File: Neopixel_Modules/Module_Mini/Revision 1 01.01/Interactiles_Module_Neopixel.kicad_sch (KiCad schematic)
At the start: 29 parts, among them J1 PINHD_1x2_Male, J2 PINHD_1x2_Female, J4 PINHD_1x2_Female, U1 MCP23017_ML

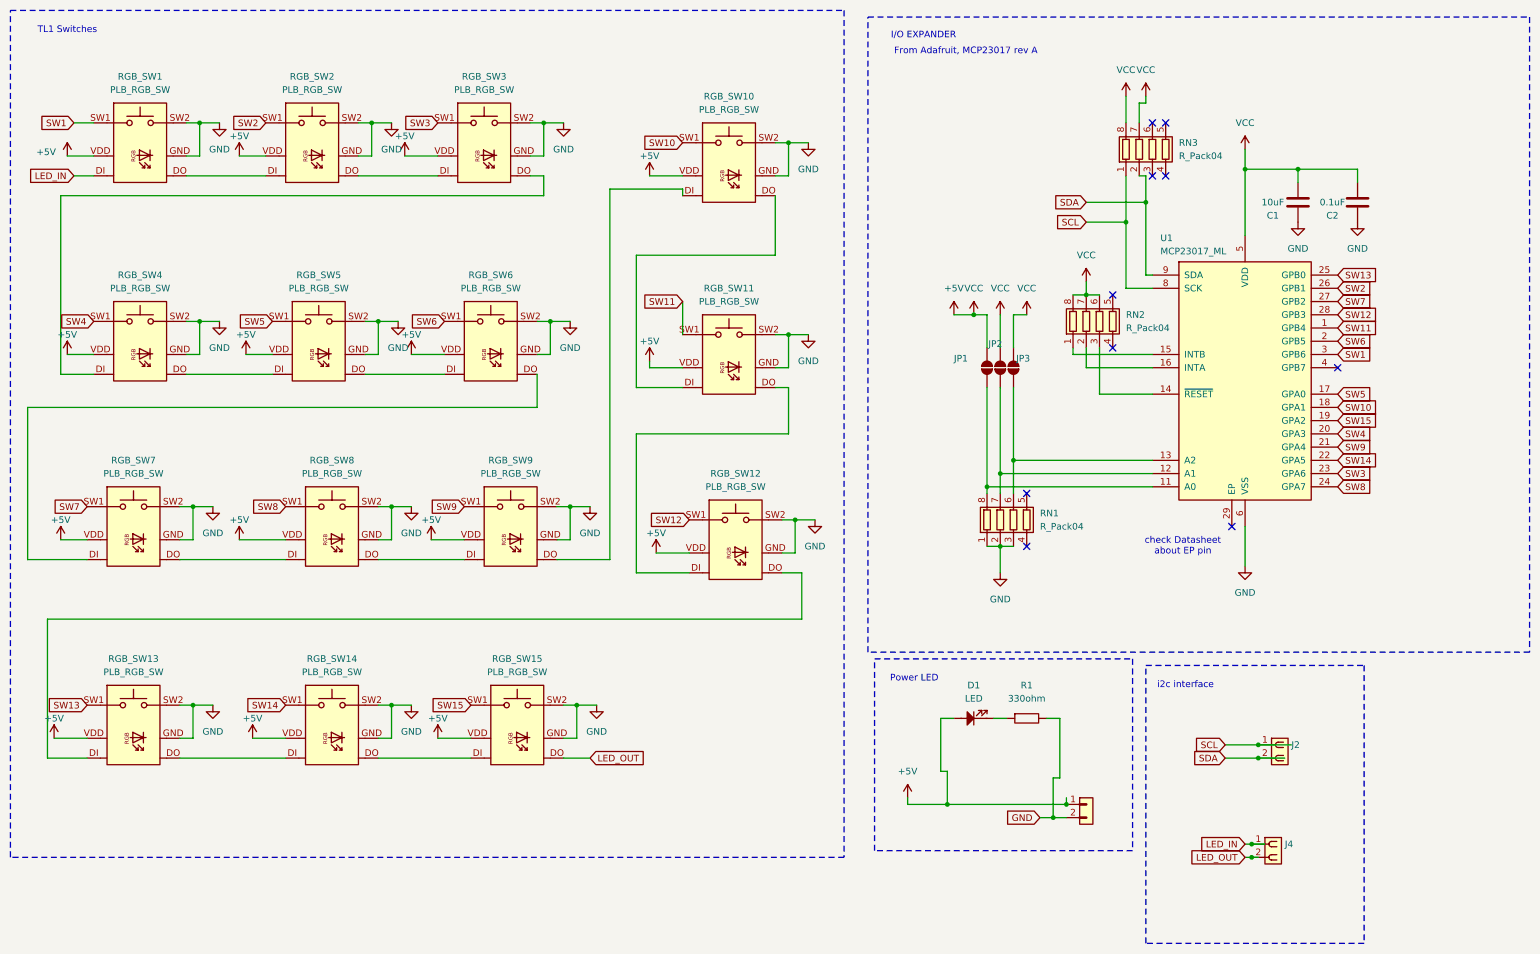
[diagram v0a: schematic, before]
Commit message: PCB Revisions
MCP23017 had incorrect footprints, some tolerances between pads were too tight (shorts), resized some components
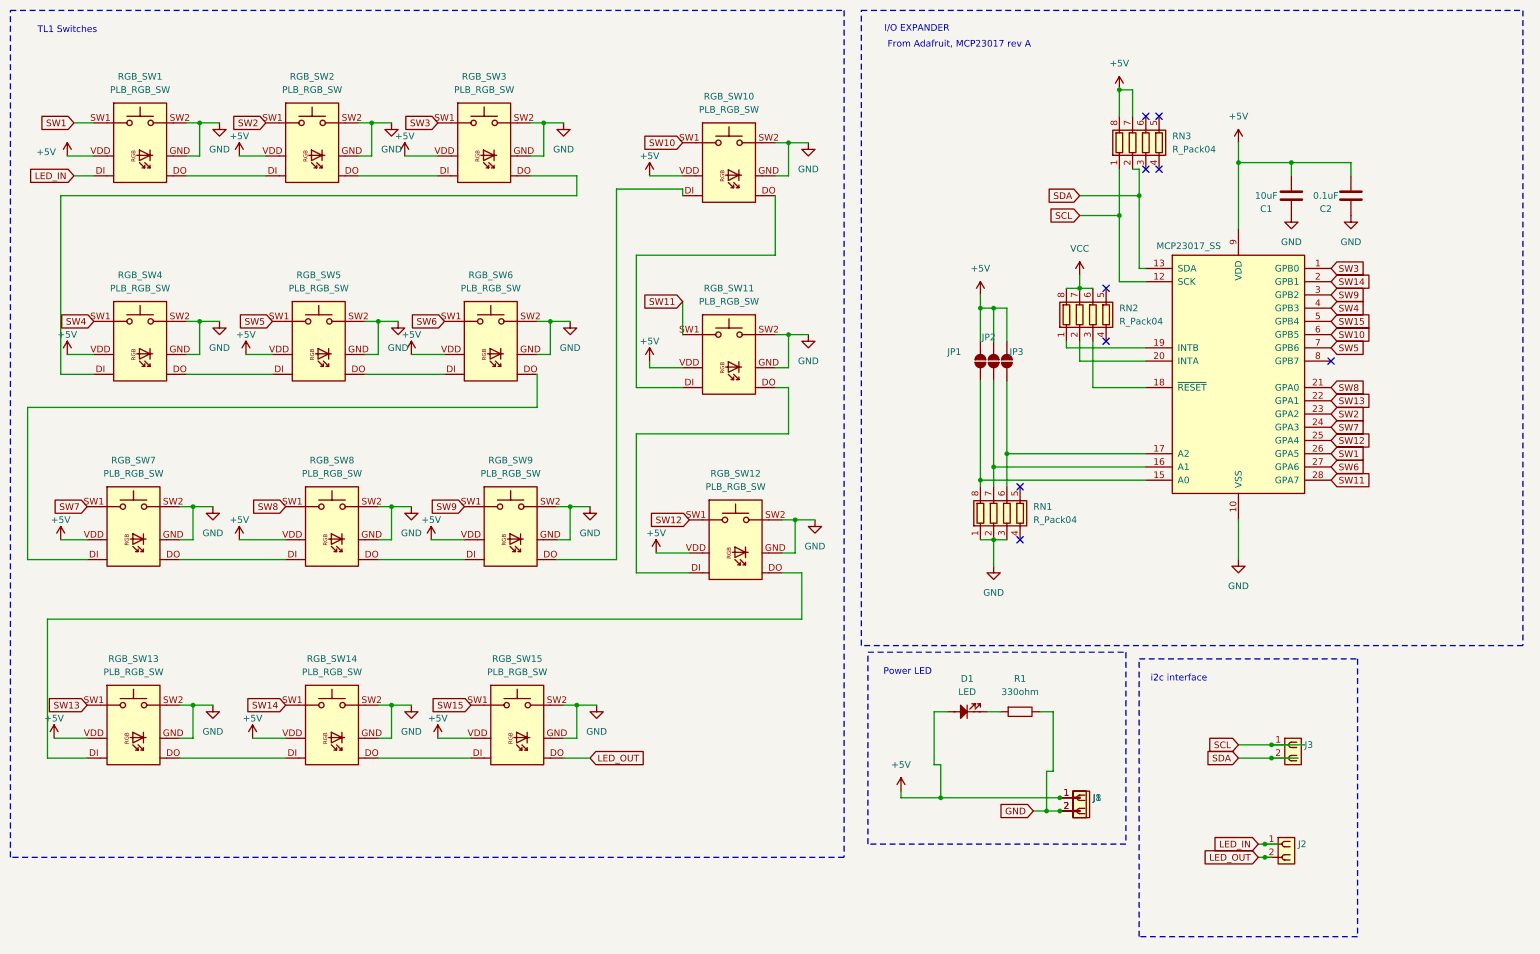
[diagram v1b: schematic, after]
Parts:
- removed J4: PINHD_1x2_Female, Connector_PinHeader_2.00mm:PinHeader_1x02_P2.00mm_Vertical, symbol PCM_SL_Pin_Headers:PINHD_1x2_Female
- removed U1: MCP23017_ML, Package_SO:SSOP-28_3.9x9.9mm_P0.635mm, symbol Interface_Expansion:MCP23017_ML
- added J3: PINHD_1x2_Female, Connector_PinHeader_2.00mm:PinHeader_1x02_P2.00mm_Vertical, symbol PCM_SL_Pin_Headers:PINHD_1x2_Female
- added J8: PINHD_1x2_Female, Connector_PinHeader_1.27mm:PinHeader_1x02_P1.27mm_Vertical, symbol PCM_SL_Pin_Headers:PINHD_1x2_Female
- added U2: MCP23017_SS, Package_SO:SSOP-28_5.3x10.2mm_P0.65mm, symbol Interface_Expansion:MCP23017_SS
- C1: footprint Capacitor_SMD:C_0603_1608Metric_Pad1.08x0.95mm_HandSolder -> Capacitor_SMD:C_0805_2012Metric_Pad1.18x1.45mm_HandSolder
- D1: footprint LED_SMD:LED_1206_3216Metric_Pad1.42x1.75mm_HandSolder -> LED_SMD:LED_0603_1608Metric_Pad1.05x0.95mm_HandSolder
- J1: footprint Connector_PinHeader_2.00mm:PinHeader_1x02_P2.00mm_Vertical -> Connector_Molex:Molex_PicoBlade_53261-0271_1x02-1MP_P1.25mm_Horizontal
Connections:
- net +5V: now also J8.1, U2.9 (VDD); no longer RN2.6 (R3.2), RN2.7 (R2.2), RN2.8 (R1.2)
- net GND: now also J8.2, U2.10 (VSS)
- net LED_IN: now also J2.1
- net LED_OUT: now also J2.2
- net SCL: now also J3.1, U2.12 (SCK); no longer J2.1
- net SDA: now also J3.2, U2.13 (SDA); no longer J2.2
- net SW1: now also U2.26 (GPA5)
- net SW10: now also U2.6 (GPB5)
- net SW11: now also U2.28 (GPA7)
- net SW12: now also U2.25 (GPA4)
- net SW13: now also U2.22 (GPA1)
- net SW14: now also U2.2 (GPB1)
- net SW15: now also U2.5 (GPB4)
- net SW2: now also U2.23 (GPA2)
- net SW3: now also U2.1 (GPB0)
- net SW4: now also U2.4 (GPB3)
- net SW5: now also U2.7 (GPB6)
- net SW6: now also U2.27 (GPA6)
- net SW7: now also U2.24 (GPA3)
- net SW8: now also U2.21 (GPA0)
- net SW9: now also U2.3 (GPB2)
- net at JP3.1 (A), RN1.6 (R3.2): now also U2.17 (A2)
- net at JP1.1 (A), RN1.8 (R1.2): now also U2.15 (A0)
- net at RN2.1 (R1.1): now also U2.19 (INTB)
- net at RN2.2 (R2.1): now also U2.20 (INTA)
- net at RN2.3 (R3.1): now also U2.18 (~{RESET})
- net at JP2.1 (A), RN1.7 (R2.2): now also U2.16 (A1)
- new net VCC: RN2.6 (R3.2), RN2.7 (R2.2), RN2.8 (R1.2)
- no-connect marks 10 -> 9
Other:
- note removed: "check Datasheet about EP pin"
- moved on the sheet: D1, R1
